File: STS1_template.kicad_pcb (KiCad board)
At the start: 4 copper layers, 85 x 85 mm, 133 parts, among them CON1 DISCO-CON1, CON11 DISCO-CON1, CON2 DISCO-CON2, CON21 DISCO-CON2, IC1 STM32F411RET6TR, IC2 STWD100PYW83F, J1 Conn_01x01_Male, J1 Conn_01x02_Female, J10 Conn_01x01_Male, J11 Conn_01x01_Male, J12 Conn_01x01_Male, J13 Conn_01x01_Male, J14 Conn_01x01_Male, J15 Conn_01x01_Male, J16 Conn_01x01_Male, J17 Conn_01x01_Male, J18 Conn_01x01_Male, J19 Conn_01x01_Male, J2 Conn_01x05_Female, J20 Conn_01x01_Male, J21 Conn_01x01_Male, J22 Conn_01x01_Male, J23 Conn_01x01_Male, J24 Conn_01x01_Male, J25 Conn_01x01_Male, J26 Conn_01x01_Male, J27 Conn_01x01_Male, J28 Conn_01x01_Male, J29 Conn_01x01_Male, J3 Conn_01x01_Male, J30 Conn_01x01_Male, J31 Conn_01x01_Male, J32 Conn_01x01_Male, J33 Conn_01x01_Male, J34 Conn_01x01_Male, J35 Conn_01x01_Male, J36 Conn_01x01_Male, J37 Conn_01x01_Male, J38 Conn_01x01_Male, J4 Conn_01x01_Male, J41 Conn_01x01_Male, J42 Conn_01x01_Male, J43 Conn_01x01_Male, J44 Conn_01x01_Male, J45 Conn_01x01_Male, J46 Conn_01x01_Male, J47 Conn_01x01_Male, J48 Conn_01x01_Male, J49 Conn_01x01_Male, J5 Conn_01x01_Male, J50 Conn_01x01_Male, J51 Conn_01x01_Male, J52 Conn_01x01_Male, J53 Conn_01x01_Male, J6 Conn_01x01_Male, J7 Conn_01x01_Male, J8 Conn_01x01_Male, J9 Conn_01x01_Male, U1 coordinate_system, U2 TPS61288

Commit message: new template
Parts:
- removed C1, C2: 20p, Capacitor_SMD:C_0805_2012Metric
- removed C10, C11 (x2), C13, C15, C17, C19, C32, C4, C5, C7, C9: 100n, Capacitor_SMD:C_0805_2012Metric
- removed C12 (x2), C14, C16, C18, C20: 47u, Capacitor_SMD:C_0805_2012Metric
- removed C21: 47uF, Capacitor_Tantalum_SMD:CP_EIA-3216-18_Kemet-A
- removed C22: 10uF, Capacitor_SMD:C_1206_3216Metric
- removed C23: 100nF, Capacitor_SMD:C_0603_1608Metric
- removed C24: 150nF, Capacitor_SMD:C_0603_1608Metric
- removed C25: 2.2uF, Capacitor_SMD:C_0603_1608Metric
- removed C26: 39nF, Capacitor_SMD:C_0603_1608Metric
- removed C27: 82pF, Capacitor_SMD:C_0603_1608Metric
- removed C28, C29, C30, C31: 68uF, Capacitor_SMD:C_2220_5650Metric
- removed C3: 1u, Capacitor_SMD:C_0805_2012Metric
- removed C6, C8: 4.7u, Capacitor_SMD:C_0805_2012Metric
- removed CON1, CON11: DISCO-CON1, cubesatFunkmodul:Cubesatconnector
- removed CON2, CON21: DISCO-CON2, cubesatFunkmodul:Cubesatconnector
- removed D1, D2, D3 (x2), D5: LED, LED_SMD:LED_0805_2012Metric
- removed FLASH1: W25Q01JVZEIQ, W25Q01JVZEIQ:SON127P800X600X80-9N-D
- removed FRAM1: CY15B108QN-40SXI, CY15B108QN-40SXI:SOIC127P800X203-8N
- removed G***: LOGO, spaceteam:STLogo
- removed IC1: STM32F411RET6TR, STM32F411RET6TR:QFP50P1200X1200X160-64N
- removed IC2: STWD100PYW83F, SamacSys_Parts:SOT65P210X110-5N
- removed J1: Conn_01x02_Female, Connector_PinHeader_2.54mm:PinHeader_1x02_P2.54mm_Vertical
- removed J1, J10, J11, J12, J13, J14, J15, J16, J17, J18, J19, J20, J21, J22, J23, J24 (x2), J25 (x2), J26, J27, J28, J29, J3, J30, J31, J32, J33, J34, J35, J36, J37, J38, J4, J41, J42, J43, J44, J45, J46, J47, J48, J49, J5, J50, J51, J52, J53, J6, J7, J8, J9: Conn_01x01_Male, Connector_PinHeader_2.54mm:PinHeader_1x01_P2.54mm_Vertical
- removed J2: Conn_01x05_Female, Connector_PinHeader_2.54mm:PinHeader_1x05_P2.54mm_Horizontal
- removed JP1, JP2, JP3, JP4, JP5, JP6: Jumper_NC_Dual, Connector_PinHeader_2.54mm:PinHeader_1x03_P2.54mm_Vertical
- removed L1: 1uH, STS1_DCDC:XAL8080
- removed R1: 220, Resistor_SMD:R_0805_2012Metric
- removed R13: 15, Resistor_SMD:R_0805_2012Metric
- removed R2, R3, R5 (x2): 100, Resistor_SMD:R_0805_2012Metric
- removed R4 (x2): 4k7, Resistor_SMD:R_0805_2012Metric
- removed R6, R8: 48k7, Resistor_SMD:R_0603_1608Metric
- removed R7: 357k, Resistor_SMD:R_0603_1608Metric
- removed RF1: LoRa1268F30, STS1_RF:LoRa1268F30
- removed RF2: RF4463F30, STS1_RF:STS1_RF4463F30
- removed U2: TPS61288, STS1_DCDC:VQFN-HR
- added CSBI_1: Conn_02x25_Odd_Even, Connector_PinHeader_2.00mm:PinHeader_2x25_P2.00mm_Vertical, F.Cu at (116.9, 56.9)
- added CSBI_2: Conn_02x25_Odd_Even, Connector_PinHeader_2.00mm:PinHeader_2x25_P2.00mm_Vertical, F.Cu at (195.9, 63.9)
- added FID5: Fiducial, Fiducial:Fiducial_0.75mm_Mask1.5mm, B.Cu at (123.4, 58.9)
- added FID6: Fiducial, Fiducial:Fiducial_0.75mm_Mask1.5mm, B.Cu at (191.4, 58.9)
- added FID7: Fiducial, Fiducial:Fiducial_0.75mm_Mask1.5mm, B.Cu at (191.4, 105.8)
- added FID8: Fiducial, Fiducial:Fiducial_0.75mm_Mask1.5mm, B.Cu at (123.4, 109.7)
- H1, H2, H3, H4: footprint MountingHole:MountingHole_3.2mm_M3_Pad_Via -> MountingHole:MountingHole_4.3mm_M4_Pad_Via
- moved U1 14.2 mm to (167.6, 54.9)
- moved FID1 0.20 mm to (123.4, 109.7)
- moved FID3 0.12 mm to (191.4, 105.8)
- moved FID2 0.07 mm to (191.4, 58.9)
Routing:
- net VBUS: track 0.00 -> 32.0 mm
- net Net-(CSBI_2-Pad7): track 0.00 -> 2.00 mm
- net Net-(CSBI_2-Pad5): track 0.00 -> 2.00 mm
- net Net-(CSBI_2-Pad11): track 0.00 -> 2.00 mm
- net Net-(CSBI_2-Pad10): track 0.00 -> 2.00 mm
- net Net-(CSBI_1-Pad45): track 0.00 -> 2.00 mm
- net Net-(CSBI_1-Pad43): track 0.00 -> 2.00 mm
- net Net-(CSBI_1-Pad41): track 0.00 -> 2.00 mm
- net Net-(CSBI_1-Pad11): track 0.00 -> 2.00 mm
- net /STS1_connector/UCI_COBC_UART_2: track 0.00 -> 2.00 mm
- net /STS1_connector/UCI_COBC_UART_1: track 0.00 -> 2.00 mm
- net /STS1_connector/UCI_COBC_3V3: track 0.00 -> 2.00 mm
- net /STS1_connector/UART_COBC_EDU_2: track 0.00 -> 2.00 mm
- net /STS1_connector/UART_COBC_EDU_1: track 0.00 -> 2.00 mm
- net /STS1_connector/EPS_CHARGING: track 0.00 -> 2.00 mm
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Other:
- outline, holes or cut-outs redrawn
- board text added: "TU Wien Space Team STS [PCB name] [Version]"
- board text removed: "TU Wien Space Team STS [STS1 COBC Prototype] v1.0"

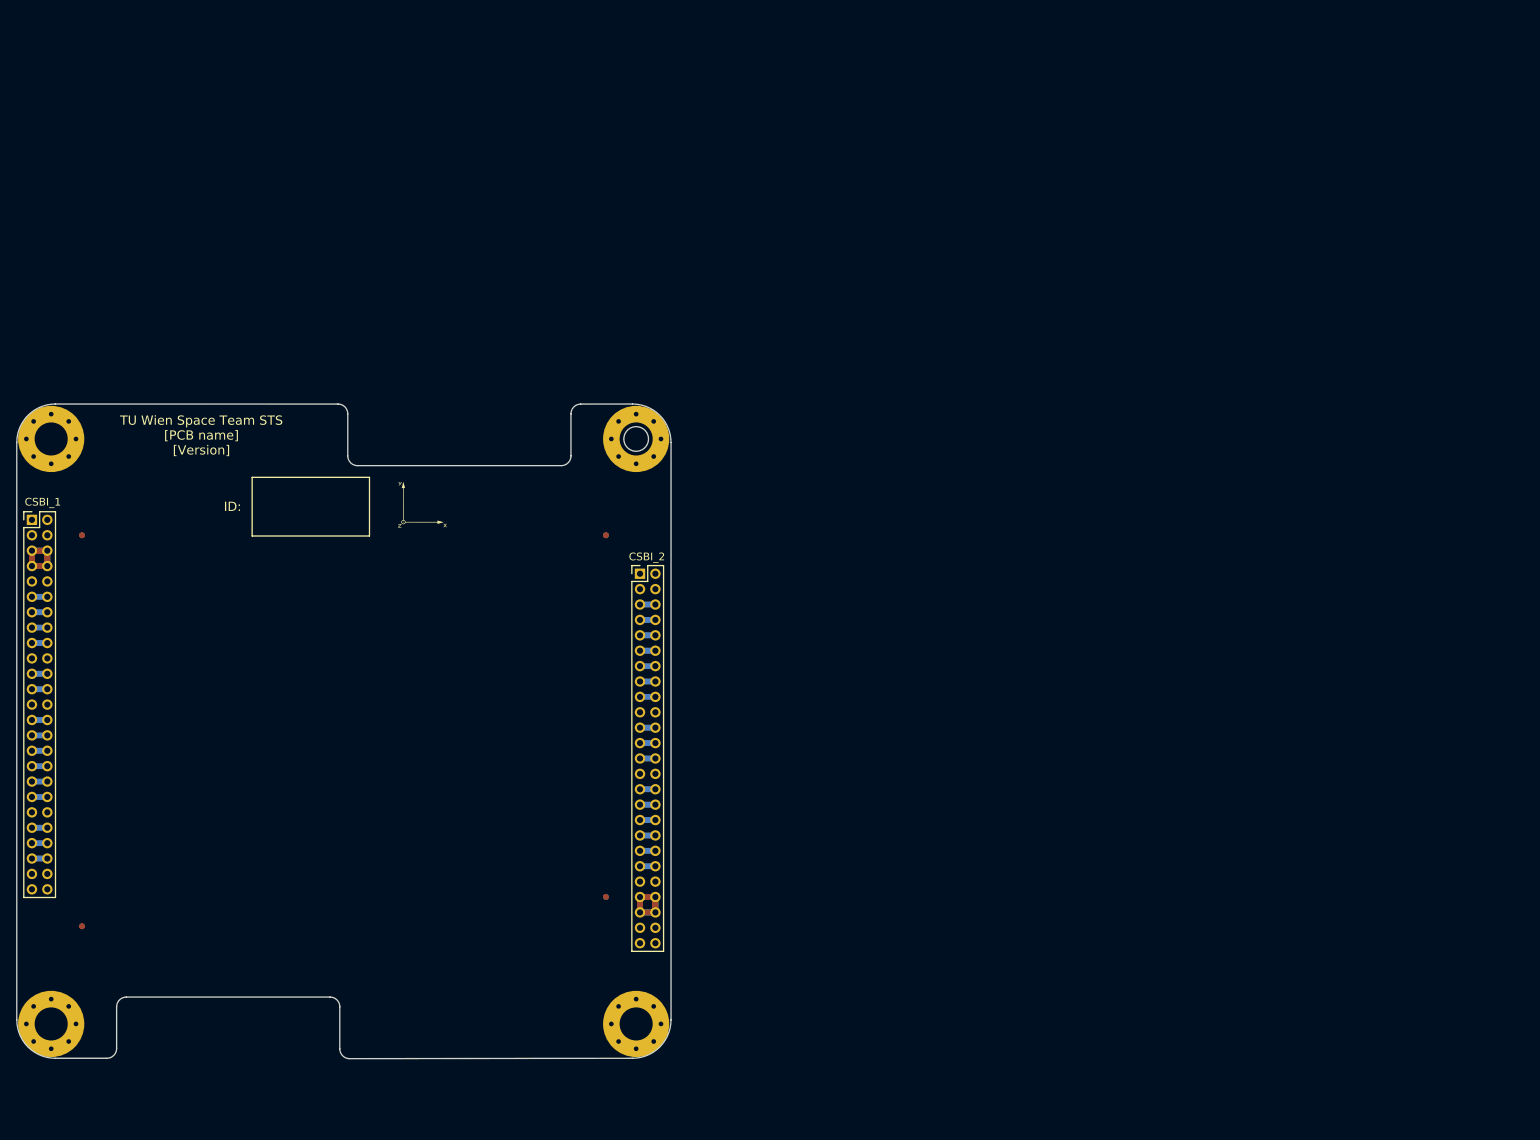
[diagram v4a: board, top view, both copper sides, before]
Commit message: component layout finished -> now wiring
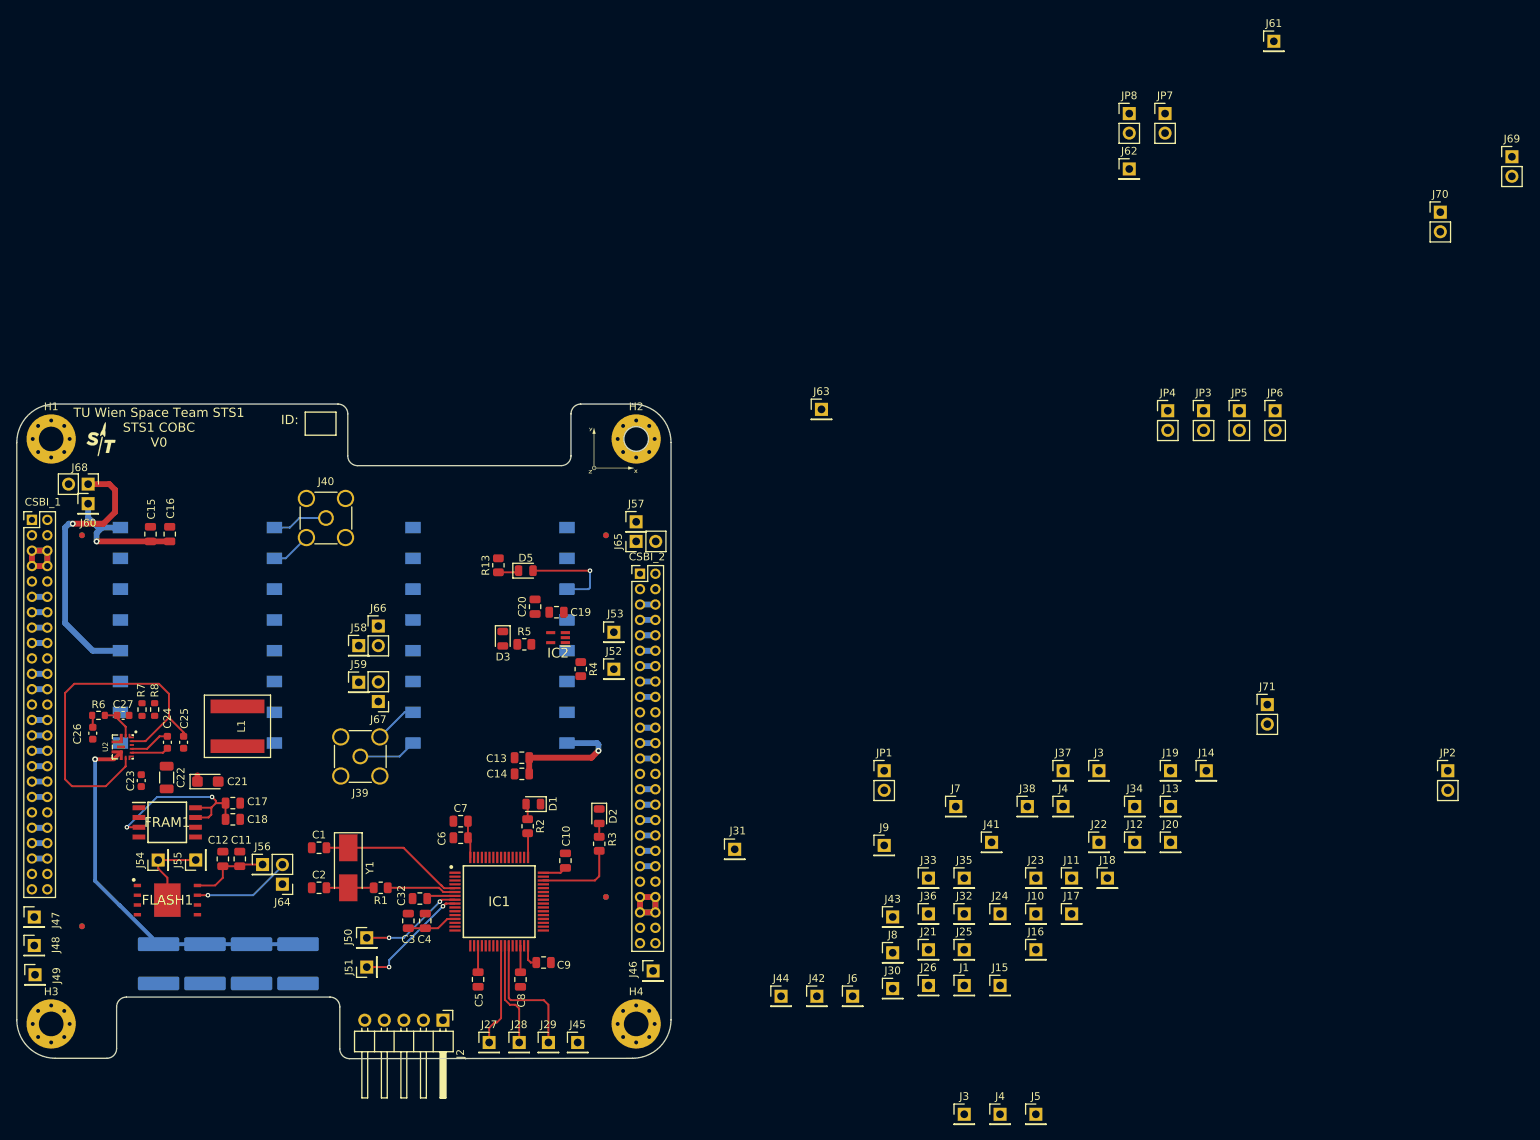
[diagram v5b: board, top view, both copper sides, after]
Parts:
- added C1: 20p, Capacitor_SMD:C_0805_2012Metric, F.Cu at (154.2, 99.5)
- added C10: 100n, Capacitor_SMD:C_0805_2012Metric, F.Cu at (186.2, 101.1)
- added C11: 100n, Capacitor_SMD:C_0805_2012Metric, F.Cu at (143.9, 100.9)
- added C12: 47u, Capacitor_SMD:C_0805_2012Metric, F.Cu at (141.7, 100.9)
- added C13: 100n, Capacitor_SMD:C_0805_2012Metric, F.Cu at (180.5, 87.8)
- added C14: 47u, Capacitor_SMD:C_0805_2012Metric, F.Cu at (180.5, 89.8)
- added C15: 100n, Capacitor_SMD:C_0805_2012Metric, F.Cu at (132.3, 58.7)
- added C16: 47u, Capacitor_SMD:C_0805_2012Metric, F.Cu at (134.8, 58.7)
- added C17: 100n, Capacitor_SMD:C_0805_2012Metric, F.Cu at (143.0, 93.7)
- added C18: 47u, Capacitor_SMD:C_0805_2012Metric, F.Cu at (143.0, 95.8)
- added C19: 100n, Capacitor_SMD:C_0805_2012Metric, F.Cu at (185.0, 68.8)
- added C2: 20p, Capacitor_SMD:C_0805_2012Metric, F.Cu at (154.2, 104.7)
- added C20: 47u, Capacitor_SMD:C_0805_2012Metric, F.Cu at (182.2, 68.1)
- added C21: 47uF, Capacitor_Tantalum_SMD:CP_EIA-3216-18_Kemet-A, F.Cu at (139.7, 90.8)
- added C22: 10uF, Capacitor_SMD:C_1206_3216Metric, F.Cu at (134.4, 90.3)
- added C23: 100nF, Capacitor_SMD:C_0603_1608Metric, F.Cu at (131.1, 90.7)
- added C24: 150nF, Capacitor_SMD:C_0603_1608Metric, F.Cu at (134.5, 85.8)
- added C25: 2.2uF, Capacitor_SMD:C_0603_1608Metric, F.Cu at (136.6, 85.8)
- added C26: 39nF, Capacitor_SMD:C_0603_1608Metric, F.Cu at (124.8, 84.6)
- added C27: 82pF, Capacitor_SMD:C_0603_1608Metric, F.Cu at (128.7, 82.2)
- added C28: 68uF, Capacitor_SMD:C_2220_5650Metric, B.Cu at (151.4, 114.5)
- added C29: 68uF, Capacitor_SMD:C_2220_5650Metric, B.Cu at (145.4, 114.5)
- added C3: 1u, Capacitor_SMD:C_0805_2012Metric, F.Cu at (165.8, 109.0)
- added C30: 68uF, Capacitor_SMD:C_2220_5650Metric, B.Cu at (139.3, 114.5)
- added C31: 68uF, Capacitor_SMD:C_2220_5650Metric, B.Cu at (133.3, 114.5)
- added C32: 100n, Capacitor_SMD:C_0805_2012Metric, F.Cu at (167.3, 106.0)
- added C4: 100n, Capacitor_SMD:C_0805_2012Metric, F.Cu at (168.0, 109.0)
- added C5: 100n, Capacitor_SMD:C_0805_2012Metric, F.Cu at (174.8, 116.6)
- added C6: 4.7u, Capacitor_SMD:C_0805_2012Metric, F.Cu at (172.6, 98.2)
- added C7: 100n, Capacitor_SMD:C_0805_2012Metric, F.Cu at (172.6, 96.0)
- added C8: 4.7u, Capacitor_SMD:C_0805_2012Metric, F.Cu at (180.3, 116.6)
- added C9: 100n, Capacitor_SMD:C_0805_2012Metric, F.Cu at (183.3, 114.4)
- added D1: LED, LED_SMD:LED_0805_2012Metric, F.Cu at (182.0, 93.8)
- added D2: LED, LED_SMD:LED_0805_2012Metric, F.Cu at (190.6, 95.3)
- added D3: LED, LED_SMD:LED_0805_2012Metric, F.Cu at (178.0, 72.3)
- added D5: LED, LED_SMD:LED_0805_2012Metric, F.Cu at (181.0, 63.5)
- added FLASH1: W25Q01JVZEIQ, W25Q01JVZEIQ:SON127P800X600X80-9N-D, F.Cu at (134.5, 106.2)
- added FRAM1: CY15B108QN-40SXI, CY15B108QN-40SXI:SOIC127P800X203-8N, F.Cu at (134.4, 96.2)
- added G***: LOGO, spaceteam:STLogoTiny, F.Cu at (125.9, 46.4)
- added IC1: STM32F411RET6TR, STM32F411RET6TR:QFP50P1200X1200X160-64N, F.Cu at (177.6, 106.5)
- added IC2: STWD100PYW83F, SamacSys_Parts:SOT65P210X110-5N, F.Cu at (185.2, 72.2)
- added J1: Conn_01x01_Male, Connector_PinHeader_2.54mm:PinHeader_1x01_P2.54mm_Vertical, F.Cu at (238.0, 117.3)
- added J10: Conn_01x01_Male, Connector_PinHeader_2.54mm:PinHeader_1x01_P2.54mm_Vertical, F.Cu at (247.3, 108.0)
- added J11: Conn_01x01_Male, Connector_PinHeader_2.54mm:PinHeader_1x01_P2.54mm_Vertical, F.Cu at (251.9, 103.4)
- added J12: Conn_01x01_Male, Connector_PinHeader_2.54mm:PinHeader_1x01_P2.54mm_Vertical, F.Cu at (260.1, 98.7)
- added J13: Conn_01x01_Male, Connector_PinHeader_2.54mm:PinHeader_1x01_P2.54mm_Vertical, F.Cu at (264.8, 94.1)
- added J14: Conn_01x01_Male, Connector_PinHeader_2.54mm:PinHeader_1x01_P2.54mm_Vertical, F.Cu at (269.4, 89.4)
- added J15: Conn_01x01_Male, Connector_PinHeader_2.54mm:PinHeader_1x01_P2.54mm_Vertical, F.Cu at (242.6, 117.3)
- added J16: Conn_01x01_Male, Connector_PinHeader_2.54mm:PinHeader_1x01_P2.54mm_Vertical, F.Cu at (247.3, 112.7)
- added J17: Conn_01x01_Male, Connector_PinHeader_2.54mm:PinHeader_1x01_P2.54mm_Vertical, F.Cu at (251.9, 108.0)
- added J18: Conn_01x01_Male, Connector_PinHeader_2.54mm:PinHeader_1x01_P2.54mm_Vertical, F.Cu at (256.6, 103.4)
- added J19: Conn_01x01_Male, Connector_PinHeader_2.54mm:PinHeader_1x01_P2.54mm_Vertical, F.Cu at (264.8, 89.4)
- added J2: Conn_01x05_Female, Connector_PinHeader_2.54mm:PinHeader_1x05_P2.54mm_Horizontal, F.Cu at (170.3, 121.8)
- added J20: Conn_01x01_Male, Connector_PinHeader_2.54mm:PinHeader_1x01_P2.54mm_Vertical, F.Cu at (264.8, 98.7)
- added J21: Conn_01x01_Male, Connector_PinHeader_2.54mm:PinHeader_1x01_P2.54mm_Vertical, F.Cu at (233.3, 112.7)
- added J22: Conn_01x01_Male, Connector_PinHeader_2.54mm:PinHeader_1x01_P2.54mm_Vertical, F.Cu at (255.5, 98.7)
- added J23: Conn_01x01_Male, Connector_PinHeader_2.54mm:PinHeader_1x01_P2.54mm_Vertical, F.Cu at (247.3, 103.4)
- added J24: Conn_01x01_Male, Connector_PinHeader_2.54mm:PinHeader_1x01_P2.54mm_Vertical, F.Cu at (242.6, 108.0)
- added J25: Conn_01x01_Male, Connector_PinHeader_2.54mm:PinHeader_1x01_P2.54mm_Vertical, F.Cu at (238.0, 112.7)
- added J26: Conn_01x01_Male, Connector_PinHeader_2.54mm:PinHeader_1x01_P2.54mm_Vertical, F.Cu at (233.3, 117.3)
- added J27: Conn_01x01_Male, Connector_PinHeader_2.54mm:PinHeader_1x01_P2.54mm_Vertical, F.Cu at (176.3, 124.8)
- added J28: Conn_01x01_Male, Connector_PinHeader_2.54mm:PinHeader_1x01_P2.54mm_Vertical, F.Cu at (180.2, 124.8)
- added J29: Conn_01x01_Male, Connector_PinHeader_2.54mm:PinHeader_1x01_P2.54mm_Vertical, F.Cu at (184.0, 124.8)
- added J3: Conn_01x01_Male, Connector_PinHeader_2.54mm:PinHeader_1x01_P2.54mm_Vertical, F.Cu at (255.5, 89.4)
- added J3: Conn_01x01_Male, Connector_PinHeader_2.54mm:PinHeader_1x01_P2.54mm_Vertical, F.Cu at (238.0, 134.1)
- added J30: Conn_01x01_Male, Connector_PinHeader_2.54mm:PinHeader_1x01_P2.54mm_Vertical, F.Cu at (228.7, 117.7)
- added J31: Conn_01x01_Male, Connector_PinHeader_2.54mm:PinHeader_1x01_P2.54mm_Vertical, F.Cu at (208.2, 99.7)
- added J32: Conn_01x01_Male, Connector_PinHeader_2.54mm:PinHeader_1x01_P2.54mm_Vertical, F.Cu at (238.0, 108.0)
- added J33: Conn_01x01_Male, Connector_PinHeader_2.54mm:PinHeader_1x01_P2.54mm_Vertical, F.Cu at (233.3, 103.4)
- added J34: Conn_01x01_Male, Connector_PinHeader_2.54mm:PinHeader_1x01_P2.54mm_Vertical, F.Cu at (260.1, 94.1)
- added J35: Conn_01x01_Male, Connector_PinHeader_2.54mm:PinHeader_1x01_P2.54mm_Vertical, F.Cu at (238.0, 103.4)
- added J36: Conn_01x01_Male, Connector_PinHeader_2.54mm:PinHeader_1x01_P2.54mm_Vertical, F.Cu at (233.3, 108.0)
- added J37: Conn_01x01_Male, Connector_PinHeader_2.54mm:PinHeader_1x01_P2.54mm_Vertical, F.Cu at (250.8, 89.4)
- added J38: Conn_01x01_Male, Connector_PinHeader_2.54mm:PinHeader_1x01_P2.54mm_Vertical, F.Cu at (246.2, 94.1)
- added J39: Conn_Coaxial, Connector_Coaxial:SMA_Amphenol_901-144_Vertical, F.Cu at (159.5, 87.6)
- added J4: Conn_01x01_Male, Connector_PinHeader_2.54mm:PinHeader_1x01_P2.54mm_Vertical, F.Cu at (250.8, 94.1)
- added J4: Conn_01x01_Male, Connector_PinHeader_2.54mm:PinHeader_1x01_P2.54mm_Vertical, F.Cu at (242.6, 134.1)
- added J40: Conn_Coaxial, Connector_Coaxial:SMA_Amphenol_901-144_Vertical, F.Cu at (155.1, 56.6)
- added J41: Conn_01x01_Male, Connector_PinHeader_2.54mm:PinHeader_1x01_P2.54mm_Vertical, F.Cu at (241.5, 98.7)
- added J42: Conn_01x01_Male, Connector_PinHeader_2.54mm:PinHeader_1x01_P2.54mm_Vertical, F.Cu at (218.8, 118.7)
- added J43: Conn_01x01_Male, Connector_PinHeader_2.54mm:PinHeader_1x01_P2.54mm_Vertical, F.Cu at (228.7, 108.4)
- added J44: Conn_01x01_Male, Connector_PinHeader_2.54mm:PinHeader_1x01_P2.54mm_Vertical, F.Cu at (214.2, 118.7)
- added J45: Conn_01x01_Male, Connector_PinHeader_2.54mm:PinHeader_1x01_P2.54mm_Vertical, F.Cu at (187.8, 124.8)
- added J46: Conn_01x01_Male, Connector_PinHeader_2.54mm:PinHeader_1x01_P2.54mm_Vertical, F.Cu at (197.6, 115.5)
- added J47: Conn_01x01_Male, Connector_PinHeader_2.54mm:PinHeader_1x01_P2.54mm_Vertical, F.Cu at (117.2, 108.5)
- added J48: Conn_01x01_Male, Connector_PinHeader_2.54mm:PinHeader_1x01_P2.54mm_Vertical, F.Cu at (117.2, 112.2)
- added J49: Conn_01x01_Male, Connector_PinHeader_2.54mm:PinHeader_1x01_P2.54mm_Vertical, F.Cu at (117.3, 116.0)
- added J5: Conn_01x01_Male, Connector_PinHeader_2.54mm:PinHeader_1x01_P2.54mm_Vertical, F.Cu at (247.3, 134.1)
- added J50: Conn_01x01_Male, Connector_PinHeader_2.54mm:PinHeader_1x01_P2.54mm_Vertical, F.Cu at (160.4, 111.2)
- added J51: Conn_01x01_Male, Connector_PinHeader_2.54mm:PinHeader_1x01_P2.54mm_Vertical, F.Cu at (160.4, 115.0)
- added J52: Conn_01x01_Male, Connector_PinHeader_2.54mm:PinHeader_1x01_P2.54mm_Vertical, F.Cu at (192.5, 76.2)
- added J53: Conn_01x01_Male, Connector_PinHeader_2.54mm:PinHeader_1x01_P2.54mm_Vertical, F.Cu at (192.5, 71.5)
- added J54: Conn_01x01_Male, Connector_PinHeader_2.54mm:PinHeader_1x01_P2.54mm_Vertical, F.Cu at (133.3, 101.0)
- added J55: Conn_01x01_Female, Connector_PinHeader_2.54mm:PinHeader_1x01_P2.54mm_Vertical, F.Cu at (138.2, 101.0)
- added J56: Conn_01x01_Male, Connector_PinHeader_2.54mm:PinHeader_1x01_P2.54mm_Vertical, F.Cu at (146.8, 101.6)
- added J57: Conn_01x01_Male, Connector_PinHeader_2.54mm:PinHeader_1x01_P2.54mm_Vertical, F.Cu at (195.4, 57.1)
- added J58: Conn_01x01_Male, Connector_PinHeader_2.54mm:PinHeader_1x01_P2.54mm_Vertical, F.Cu at (159.3, 73.2)
- added J59: Conn_01x01_Male, Connector_PinHeader_2.54mm:PinHeader_1x01_P2.54mm_Vertical, F.Cu at (159.3, 78.0)
- added J6: Conn_01x01_Male, Connector_PinHeader_2.54mm:PinHeader_1x01_P2.54mm_Vertical, F.Cu at (223.5, 118.7)
- added J60: Conn_01x01_Male, Connector_PinHeader_2.54mm:PinHeader_1x01_P2.54mm_Vertical, F.Cu at (124.2, 54.8)
- added J61: Conn_01x01_Male, Connector_PinHeader_2.54mm:PinHeader_1x01_P2.54mm_Vertical, F.Cu at (278.2, -5.32)
- added J62: Conn_01x01_Male, Connector_PinHeader_2.54mm:PinHeader_1x01_P2.54mm_Vertical, F.Cu at (259.4, 11.3)
- added J63: Conn_01x01_Male, Connector_PinHeader_2.54mm:PinHeader_1x01_P2.54mm_Vertical, F.Cu at (219.4, 42.5)
- added J64: Conn_01x02_Male, Connector_PinHeader_2.54mm:PinHeader_1x02_P2.54mm_Vertical, F.Cu at (149.4, 104.2)
- added J65: Conn_01x02_Male, Connector_PinHeader_2.54mm:PinHeader_1x02_P2.54mm_Vertical, F.Cu at (195.4, 59.6)
- added J66: Conn_01x02_Male, Connector_PinHeader_2.54mm:PinHeader_1x02_P2.54mm_Vertical, F.Cu at (161.9, 70.7)
- added J67: Conn_01x02_Male, Connector_PinHeader_2.54mm:PinHeader_1x02_P2.54mm_Vertical, F.Cu at (161.9, 80.5)
- added J68: Conn_01x02_Male, Connector_PinHeader_2.54mm:PinHeader_1x02_P2.54mm_Vertical, F.Cu at (124.2, 52.2)
- added J69: Conn_01x02_Male, Connector_PinHeader_2.54mm:PinHeader_1x02_P2.54mm_Vertical, F.Cu at (309.1, 9.68)
- added J7: Conn_01x01_Male, Connector_PinHeader_2.54mm:PinHeader_1x01_P2.54mm_Vertical, F.Cu at (236.9, 94.1)
- added J70: Conn_01x02_Male, Connector_PinHeader_2.54mm:PinHeader_1x02_P2.54mm_Vertical, F.Cu at (299.8, 16.9)
- added J71: Conn_01x02_Male, Connector_PinHeader_2.54mm:PinHeader_1x02_P2.54mm_Vertical, F.Cu at (277.4, 80.8)
- added J8: Conn_01x01_Male, Connector_PinHeader_2.54mm:PinHeader_1x01_P2.54mm_Vertical, F.Cu at (228.7, 113.1)
- added J9: Conn_01x01_Male, Connector_PinHeader_2.54mm:PinHeader_1x01_P2.54mm_Vertical, F.Cu at (227.6, 99.1)
- added JP1: Jumper_NC_Dual, Connector_PinHeader_2.54mm:PinHeader_1x02_P2.54mm_Vertical, F.Cu at (227.6, 89.4)
- added JP2: Jumper_NC_Dual, Connector_PinHeader_2.54mm:PinHeader_1x02_P2.54mm_Vertical, F.Cu at (300.8, 89.4)
- added JP3: Jumper_NC_Dual, Connector_PinHeader_2.54mm:PinHeader_1x02_P2.54mm_Vertical, F.Cu at (269.1, 42.7)
- added JP4: Jumper_NC_Dual, Connector_PinHeader_2.54mm:PinHeader_1x02_P2.54mm_Vertical, F.Cu at (264.4, 42.7)
- added JP5: Jumper_NC_Dual, Connector_PinHeader_2.54mm:PinHeader_1x02_P2.54mm_Vertical, F.Cu at (273.7, 42.7)
- added JP6: Jumper_NC_Dual, Connector_PinHeader_2.54mm:PinHeader_1x02_P2.54mm_Vertical, F.Cu at (278.4, 42.7)
- added JP7: Jumper_NC_Dual, Connector_PinHeader_2.54mm:PinHeader_1x02_P2.54mm_Vertical, F.Cu at (264.1, 4.07)
- added JP8: Jumper_NC_Dual, Connector_PinHeader_2.54mm:PinHeader_1x02_P2.54mm_Vertical, F.Cu at (259.4, 4.07)
- added L1: 1uH, STS1_DCDC:XAL8080, F.Cu at (143.6, 83.7)
- added R1: 220, Resistor_SMD:R_0805_2012Metric, F.Cu at (162.2, 104.7)
- added R13: 15, Resistor_SMD:R_0805_2012Metric, F.Cu at (177.5, 62.8)
- added R2: 100, Resistor_SMD:R_0805_2012Metric, F.Cu at (181.3, 96.7)
- added R3: 100, Resistor_SMD:R_0805_2012Metric, F.Cu at (190.6, 98.9)
- added R4: 4k7, Resistor_SMD:R_0805_2012Metric, F.Cu at (188.2, 76.2)
- added R5: 100, Resistor_SMD:R_0805_2012Metric, F.Cu at (180.8, 73.0)
- added R6: 48k7, Resistor_SMD:R_0603_1608Metric, F.Cu at (125.5, 82.2)
- added R7: 357k, Resistor_SMD:R_0603_1608Metric, F.Cu at (131.2, 81.5)
- added R8: 48k7, Resistor_SMD:R_0603_1608Metric, F.Cu at (132.8, 81.5)
- added RF1: LoRa1268F30, STS1_RF:LoRa1268F30, B.Cu at (186.4, 85.8)
- added RF2: RF4463F30, STS1_RF:STS1_RF4463F30, B.Cu at (128.4, 57.9)
- added U2: TPS61288, STS1_DCDC:VQFN-HR, F.Cu at (128.7, 86.3)
- added Y1: 12MHz, Crystal:Crystal_SMD_5032-2Pin_5.0x3.2mm_HandSoldering, F.Cu at (158.0, 102.0)
- H1, H2, H3, H4: footprint MountingHole:MountingHole_4.3mm_M4_Pad_Via -> MountingHole:MountingHole_3.2mm_M3_Pad_Via
- moved U1 25.8 mm to (192.4, 47.9)
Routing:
- net +5V: track 0.00 -> 84.0 mm, vias 0 -> 3
- net +3V3: track 0.00 -> 56.2 mm, vias 0 -> 2
- net Net-(C25-Pad1): track 0.00 -> 48.6 mm
- net Net-(J68-Pad1): track 0.00 -> 35.1 mm, vias 0 -> 1
- net Net-(C1-Pad2): track 0.00 -> 18.9 mm
- net Net-(IC1-Pad27): track 0.00 -> 17.2 mm
- net /STS1_COBC_uC/PC1: track 0.00 -> 15.4 mm, vias 0 -> 2
- net Net-(IC1-Pad26): track 0.00 -> 13.7 mm
- net /STS1_COBC_uC/PC0: track 0.00 -> 13.5 mm, vias 0 -> 2
- net Net-(IC1-Pad25): track 0.00 -> 13.4 mm
- net Net-(FLASH1-Pad7): track 0.00 -> 12.8 mm, vias 0 -> 1
- net Net-(D5-Pad2): track 0.00 -> 12.7 mm, vias 0 -> 1
- net Net-(IC1-Pad46): track 0.00 -> 10.8 mm
- net Net-(FLASH1-Pad9): track 0.00 -> 10.6 mm
- net Net-(IC1-Pad6): track 0.00 -> 8.96 mm
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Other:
- board text added: "TU Wien Space Team STS1 STS1 COBC V0"
- board text removed: "TU Wien Space Team STS [PCB name] [Version]"
